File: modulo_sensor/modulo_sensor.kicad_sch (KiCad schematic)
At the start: 33 parts, among them J1 Conn_01x08_Pin, U1 74HC14DR2G

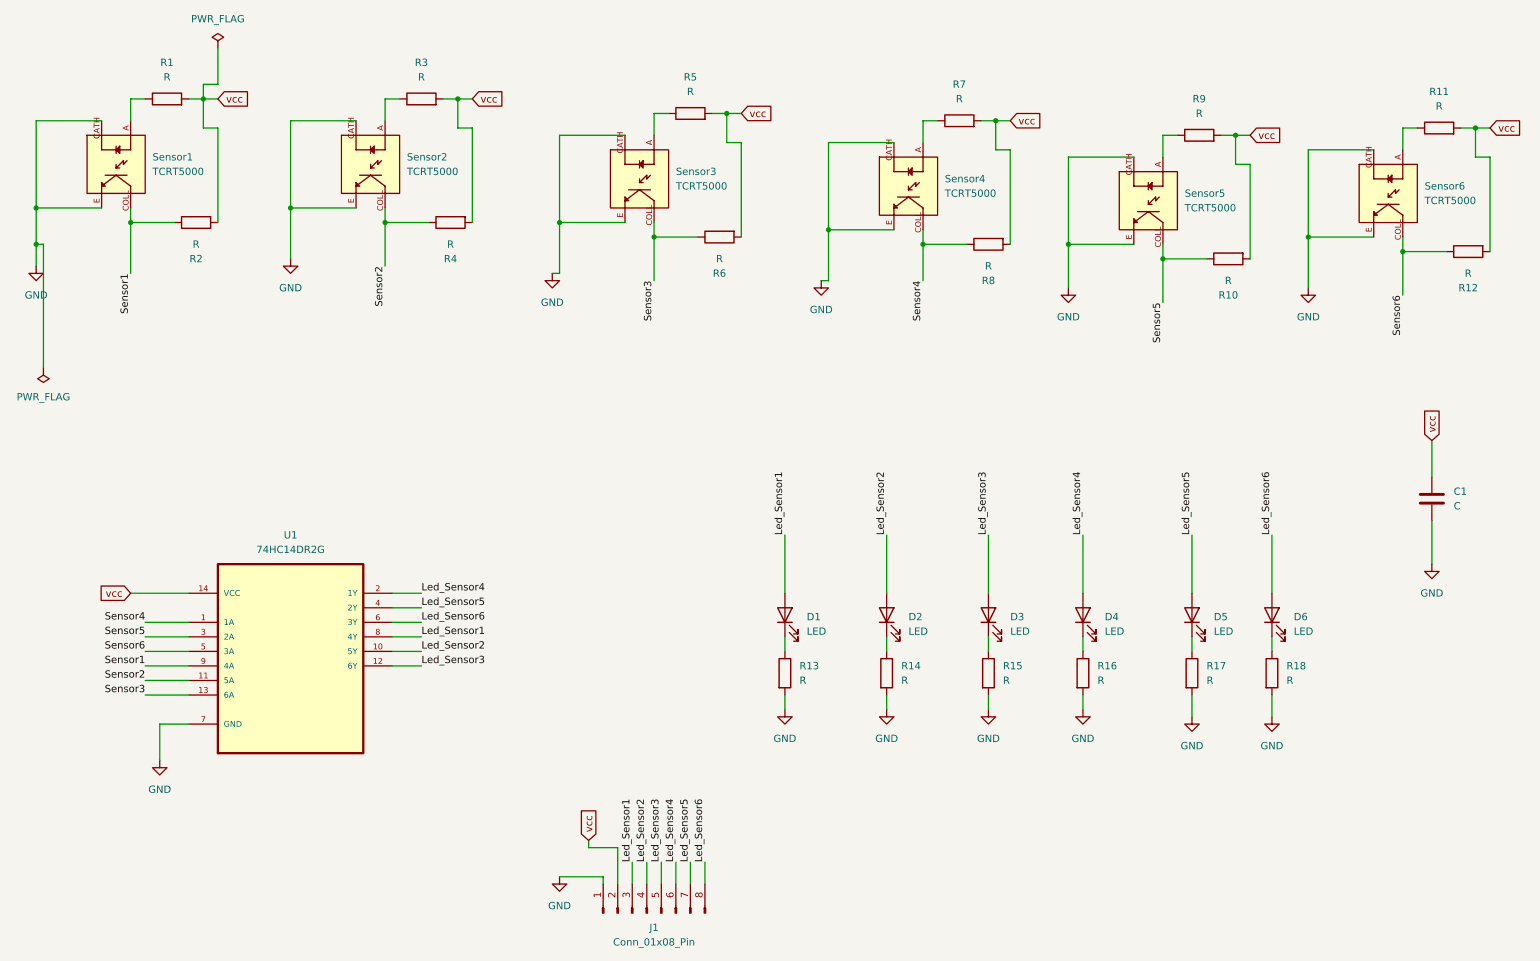
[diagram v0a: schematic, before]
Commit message: fix: Actualizo los valores de las resistencias y el footprint del led
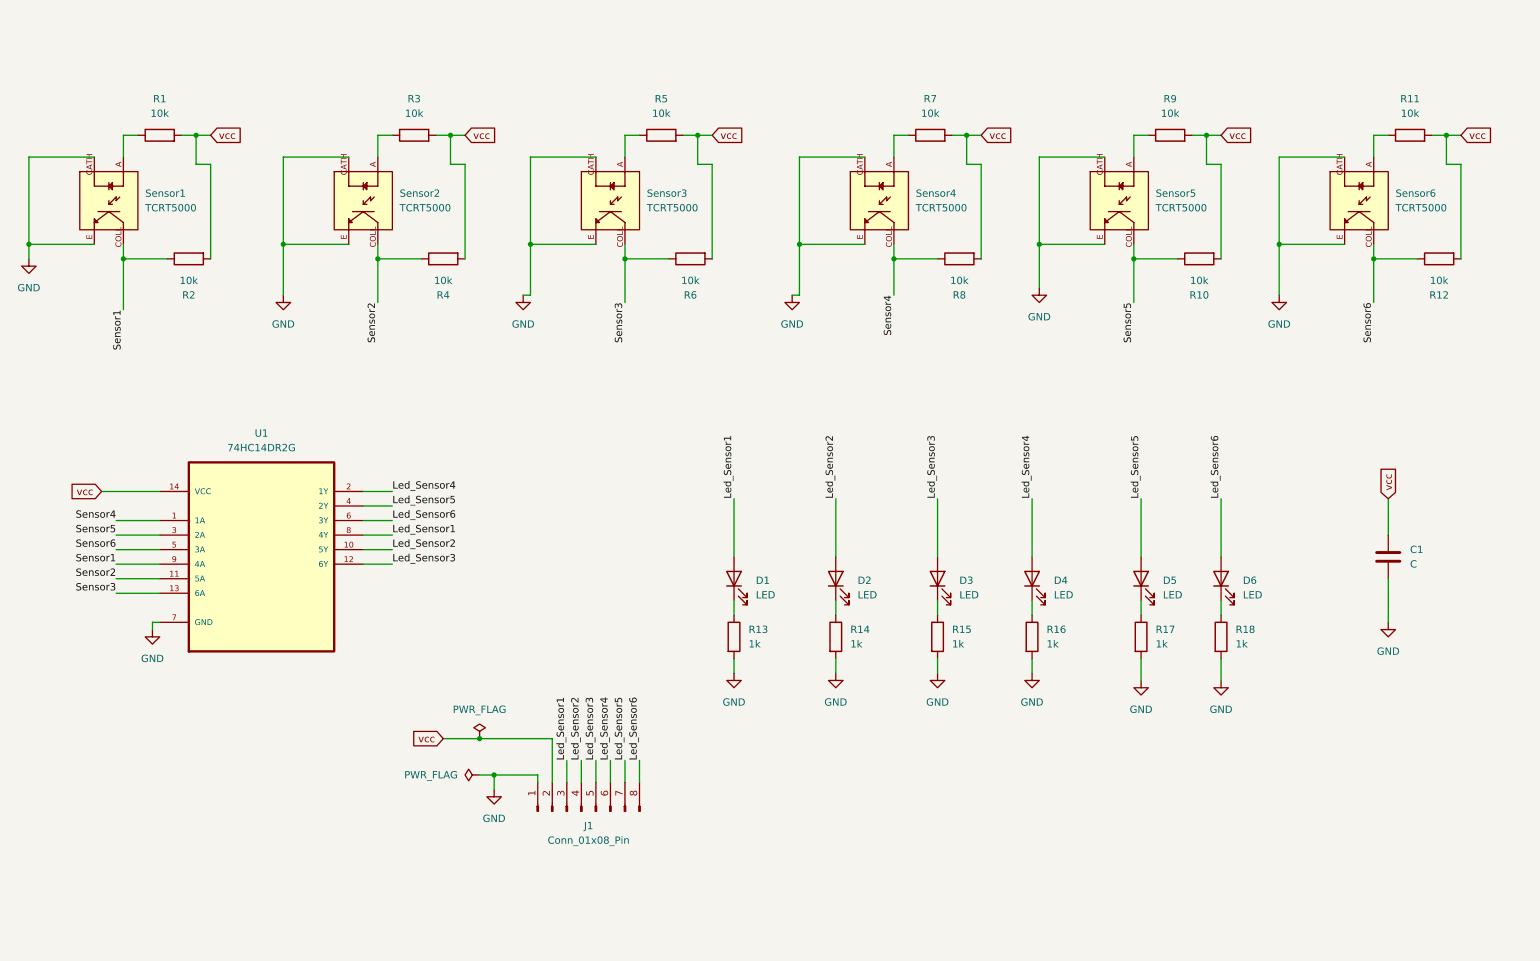
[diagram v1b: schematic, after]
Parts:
- D1: footprint LED_THT:LED_D1.8mm_W3.3mm_H2.4mm -> LED_THT:LED_D3.0mm
- R1, R10, R11, R12, R2, R3, R4, R5, R6, R7, R8, R9: value R -> 10k
- R13, R14, R15, R16, R17, R18: value R -> 1k
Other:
- moved on the sheet: C1, D1, D2, D3, D4, D5, D6, J1, R1, R10, R11, R12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

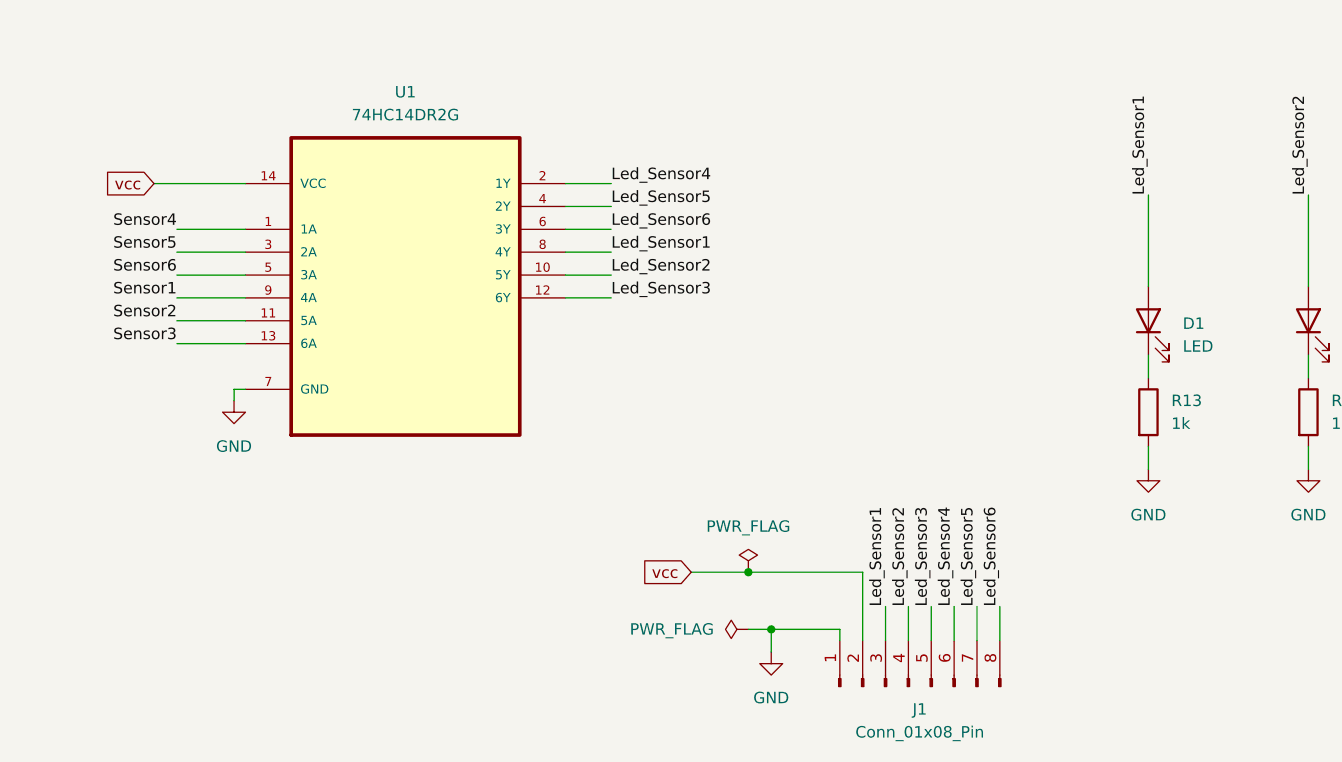
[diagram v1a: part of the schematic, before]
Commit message: refactor: Intercambio los labels de los pines y del 74HC para acomodarlos en la pcb
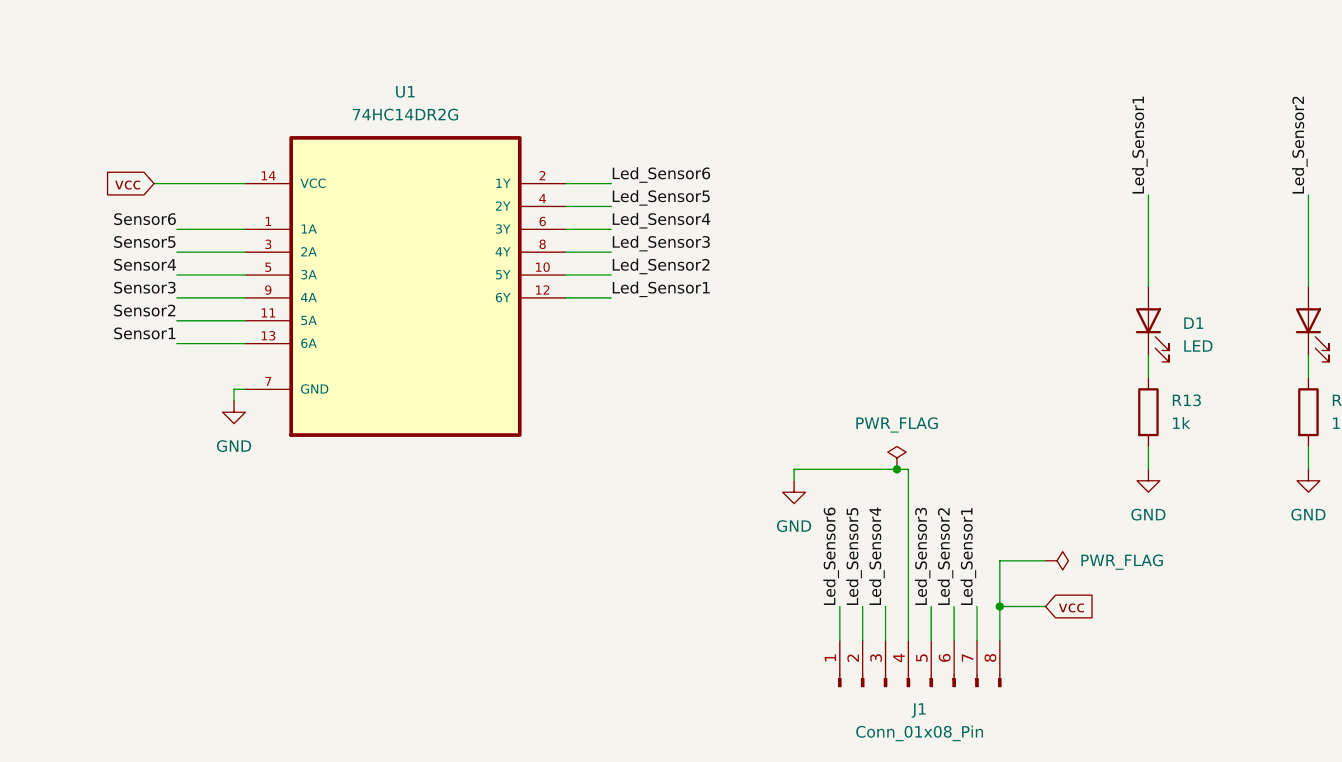
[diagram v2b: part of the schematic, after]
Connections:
- net GND: now also J1.4 (Pin_4); no longer J1.1 (Pin_1)
- net Led_Sensor1: now also J1.7 (Pin_7), U1.12 (6Y); no longer J1.3 (Pin_3), U1.8 (4Y)
- net Led_Sensor2: now also J1.6 (Pin_6); no longer J1.4 (Pin_4)
- net Led_Sensor3: now also U1.8 (4Y); no longer U1.12 (6Y)
- net Led_Sensor4: now also J1.3 (Pin_3), U1.6 (3Y); no longer J1.6 (Pin_6), U1.2 (1Y)
- net Led_Sensor5: now also J1.2 (Pin_2); no longer J1.7 (Pin_7)
- net Led_Sensor6: now also J1.1 (Pin_1), U1.2 (1Y); no longer J1.8 (Pin_8), U1.6 (3Y)
- net Sensor1: now also U1.13 (6A); no longer U1.9 (4A)
- net Sensor3: now also U1.9 (4A); no longer U1.13 (6A)
- net Sensor4: now also U1.5 (3A); no longer U1.1 (1A)
- net Sensor6: now also U1.1 (1A); no longer U1.5 (3A)
- net vcc: now also J1.8 (Pin_8); no longer J1.2 (Pin_2)

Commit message: refactor: Cambio los footprints de todas las resistencias THT por SMD
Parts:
- R1, R10, R11, R12, R13, R14, R15, R16, R17, R18, R2, R3, R4, R5, R6, R7, R8, R9: footprint Resistor_THT:R_Axial_DIN0204_L3.6mm_D1.6mm_P5.08mm_Horizontal -> Resistor_SMD:R_0805_2012Metric_Pad1.20x1.40mm_HandSolder
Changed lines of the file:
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@@
 			)
 		)
-		(property "Footprint" "Resistor_THT:R_Axial_DIN0204_L3.6mm_D1.6mm_P5.08mm_Horizontal"
+		(property "Footprint" "Resistor_SMD:R_0805_2012Metric_Pad1.20x1.40mm_HandSolder"
 			(at 225.552 130.81 90)
 			(effects
@@
 			)
 		)
-		(property "Footprint" "Resistor_THT:R_Axial_DIN0204_L3.6mm_D1.6mm_P5.08mm_Horizontal"
+		(property "Footprint" "Resistor_SMD:R_0805_2012Metric_Pad1.20x1.40mm_HandSolder"
 			(at 86.36 44.958 90)
 			(effects
@@
 			)
 		)
-		(property "Footprint" "Resistor_THT:R_Axial_DIN0204_L3.6mm_D1.6mm_P5.08mm_Horizontal"
+		(property "Footprint" "Resistor_SMD:R_0805_2012Metric_Pad1.20x1.40mm_HandSolder"
 			(at 158.242 130.81 90)
 			(effects
@@
 			)
 		)
-		(property "Footprint" "Resistor_THT:R_Axial_DIN0204_L3.6mm_D1.6mm_P5.08mm_Horizontal"
+		(property "Footprint" "Resistor_SMD:R_0805_2012Metric_Pad1.20x1.40mm_HandSolder"
 			(at 140.462 130.81 90)
 			(effects
@@
 			)
 		)
-		(property "Footprint" "Resistor_THT:R_Axial_DIN0204_L3.6mm_D1.6mm_P5.08mm_Horizontal"
+		(property "Footprint" "Resistor_SMD:R_0805_2012Metric_Pad1.20x1.40mm_HandSolder"
 			(at 181.61 62.992 90)
 			(effects
@@
 			)
 		)
-		(property "Footprint" "Resistor_THT:R_Axial_DIN0204_L3.6mm_D1.6mm_P5.08mm_Horizontal"
+		(property "Footprint" "Resistor_SMD:R_0805_2012Metric_Pad1.20x1.40mm_HandSolder"
 			(at 134.62 62.992 90)
 			(effects
@@
 			)
 		)
-		(property "Footprint" "Resistor_THT:R_Axial_DIN0204_L3.6mm_D1.6mm_P5.08mm_Horizontal"
+		(property "Footprint" "Resistor_SMD:R_0805_2012Metric_Pad1.20x1.40mm_HandSolder"
 			(at 223.52 62.992 90)
 			(effects
@@
 			)
 		)
-		(property "Footprint" "Resistor_THT:R_Axial_DIN0204_L3.6mm_D1.6mm_P5.08mm_Horizontal"
+		(property "Footprint" "Resistor_SMD:R_0805_2012Metric_Pad1.20x1.40mm_HandSolder"
 			(at 176.022 130.81 90)
 			(effects
@@
 			)
 		)
-		(property "Footprint" "Resistor_THT:R_Axial_DIN0204_L3.6mm_D1.6mm_P5.08mm_Horizontal"
+		(property "Footprint" "Resistor_SMD:R_0805_2012Metric_Pad1.20x1.40mm_HandSolder"
 			(at 91.44 62.992 90)
 			(effects
@@
 			)
 		)
-		(property "Footprint" "Resistor_THT:R_Axial_DIN0204_L3.6mm_D1.6mm_P5.08mm_Horizontal"
+		(property "Footprint" "Resistor_SMD:R_0805_2012Metric_Pad1.20x1.40mm_HandSolder"
 			(at 176.53 44.958 90)
 			(effects
@@
 			)
 		)
-		(property "Footprint" "Resistor_THT:R_Axial_DIN0204_L3.6mm_D1.6mm_P5.08mm_Horizontal"
+		(property "Footprint" "Resistor_SMD:R_0805_2012Metric_Pad1.20x1.40mm_HandSolder"
 			(at 41.91 44.958 90)
 			(effects
@@
 			)
 		)
-		(property "Footprint" "Resistor_THT:R_Axial_DIN0204_L3.6mm_D1.6mm_P5.08mm_Horizontal"
+		(property "Footprint" "Resistor_SMD:R_0805_2012Metric_Pad1.20x1.40mm_HandSolder"
 			(at 260.35 44.958 90)
 			(effects
@@
 			)
 		)
-		(property "Footprint" "Resistor_THT:R_Axial_DIN0204_L3.6mm_D1.6mm_P5.08mm_Horizontal"
+		(property "Footprint" "Resistor_SMD:R_0805_2012Metric_Pad1.20x1.40mm_HandSolder"
 			(at 211.582 130.81 90)
 			(effects
@@
 			)
 		)
-		(property "Footprint" "Resistor_THT:R_Axial_DIN0204_L3.6mm_D1.6mm_P5.08mm_Horizontal"
+		(property "Footprint" "Resistor_SMD:R_0805_2012Metric_Pad1.20x1.40mm_HandSolder"
 			(at 129.54 44.958 90)
 			(effects
@@
 			)
 		)
-		(property "Footprint" "Resistor_THT:R_Axial_DIN0204_L3.6mm_D1.6mm_P5.08mm_Horizontal"
+		(property "Footprint" "Resistor_SMD:R_0805_2012Metric_Pad1.20x1.40mm_HandSolder"
 			(at 218.44 44.958 90)
 			(effects
@@
 			)
 		)
-		(property "Footprint" "Resistor_THT:R_Axial_DIN0204_L3.6mm_D1.6mm_P5.08mm_Horizontal"
+		(property "Footprint" "Resistor_SMD:R_0805_2012Metric_Pad1.20x1.40mm_HandSolder"
 			(at 46.99 62.992 90)
 			(effects
@@
 			)
 		)
-		(property "Footprint" "Resistor_THT:R_Axial_DIN0204_L3.6mm_D1.6mm_P5.08mm_Horizontal"
+		(property "Footprint" "Resistor_SMD:R_0805_2012Metric_Pad1.20x1.40mm_HandSolder"
 			(at 192.532 130.81 90)
 			(effects
@@
 			)
 		)
-		(property "Footprint" "Resistor_THT:R_Axial_DIN0204_L3.6mm_D1.6mm_P5.08mm_Horizontal"
+		(property "Footprint" "Resistor_SMD:R_0805_2012Metric_Pad1.20x1.40mm_HandSolder"
 			(at 265.43 62.992 90)
 			(effects

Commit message: fix: Cambio las huellas de los leds por smd en el esquemático
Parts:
- D1, D2, D3, D4, D5, D6: footprint LED_THT:LED_D3.0mm -> LED_SMD:LED_1206_3216Metric_Pad1.42x1.75mm_HandSolder
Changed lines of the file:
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@@
 			)
 		)
-		(property "Footprint" "LED_THT:LED_D3.0mm"
+		(property "Footprint" "LED_SMD:LED_1206_3216Metric_Pad1.42x1.75mm_HandSolder"
 			(at 177.8 120.65 0)
 			(effects
@@
 			)
 		)
-		(property "Footprint" "LED_THT:LED_D3.0mm"
+		(property "Footprint" "LED_SMD:LED_1206_3216Metric_Pad1.42x1.75mm_HandSolder"
 			(at 194.31 120.65 0)
 			(effects
@@
 			)
 		)
-		(property "Footprint" "LED_THT:LED_D3.0mm"
+		(property "Footprint" "LED_SMD:LED_1206_3216Metric_Pad1.42x1.75mm_HandSolder"
 			(at 160.02 120.65 0)
 			(effects
@@
 			)
 		)
-		(property "Footprint" "LED_THT:LED_D3.0mm"
+		(property "Footprint" "LED_SMD:LED_1206_3216Metric_Pad1.42x1.75mm_HandSolder"
 			(at 227.33 120.65 0)
 			(effects
@@
 			)
 		)
-		(property "Footprint" "LED_THT:LED_D3.0mm"
+		(property "Footprint" "LED_SMD:LED_1206_3216Metric_Pad1.42x1.75mm_HandSolder"
 			(at 213.36 120.65 0)
 			(effects
@@
 			)
 		)
-		(property "Footprint" "LED_THT:LED_D3.0mm"
+		(property "Footprint" "LED_SMD:LED_1206_3216Metric_Pad1.42x1.75mm_HandSolder"
 			(at 142.24 120.65 0)
 			(effects
